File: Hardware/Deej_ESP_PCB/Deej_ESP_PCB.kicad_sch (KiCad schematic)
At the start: 124 parts, among them J1 USB_C_Receptacle_USB2.0_16P, P1 10K, P2 10K, P3 10K, P4 10K, P5 10K, P6 10K, SW1 SW_Push, SW2 SW_Push, SW3 SW_Push, SW4 SW_Push, SW5 SW_Push, SW6 SW_Push, U1 ESP32-S3-MINI-1U, U11 ECMF02-2AMX6, U12 LMS1585ACS-3.3/NOPB, U15 1.3" 128x64 OLED, U2 PCF8574RGTR, U3 PCF8574RGTR, U4 PCF8574RGTR, U5 SN74HCS126DR, U6 SN74HCS126DR, U7 1.3" 128x64 OLED, U8 1.3" 128x64 OLED, U9 1.3" 128x64 OLED

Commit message: Migrated Project Footprints to KiCAD Stable
- I updated the project footprints to be compatable with KiCAD stable
  release.
- I replaced the footprint for the slide potentiometer.
- I corrected the Adafruit display in the BOM sheet since I swapped it
  out a few commits ago.
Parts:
- P1, P2, P3, P4, P5, P6: footprint Bourns_Potentiometer:PTL01 -> Bourns_Potentiometer:PTL0115R0103B1

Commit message: Still dealing with KiCAD Migration issues
- Had to spend way too much time fixing the libraries.
- Adjusted the Adafruit 1.3" OLED footprint 3D model to use a lower
  profile pin headder.
- Added the lower profile pins to the BOM.
- Went through some of the ERC and fixed some issues (most relating to
  the library issues mentioned above).
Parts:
- removed D25: Green LED, LED_SMD:LED_0603_1608Metric_Pad1.05x0.95mm_HandSolder, symbol Device:LED
- removed R29: 100, Capacitor_SMD:C_0603_1608Metric_Pad1.08x0.95mm_HandSolder, symbol Device:R
- removed U2, U3, U4: PCF8574RGTR, RGT16_1P6X1P6, symbol TI:PCF8574RGTR
- CR1: renamed from CR17; footprint QFN1610_STM -> STM:QFN-6L_STM
- CR10: renamed from CR2; footprint DIODE_ESDALC6V1-1U2_STM -> STM:DIODE_ESDALC6V1-1U2_STM
- CR11: renamed from CR1; footprint DIODE_ESDALC6V1-1U2_STM -> STM:DIODE_ESDALC6V1-1U2_STM
- CR12: renamed from CR11; footprint DIODE_ESDALC6V1-1U2_STM -> STM:DIODE_ESDALC6V1-1U2_STM
- CR13: renamed from CR12; footprint DIODE_ESDALC6V1-1U2_STM -> STM:DIODE_ESDALC6V1-1U2_STM
- CR14: renamed from CR13; footprint DIODE_ESDALC6V1-1U2_STM -> STM:DIODE_ESDALC6V1-1U2_STM
- CR15: renamed from CR14; footprint DIODE_ESDALC6V1-1U2_STM -> STM:DIODE_ESDALC6V1-1U2_STM
- CR16: renamed from CR15; footprint DIODE_ESDALC6V1-1U2_STM -> STM:DIODE_ESDALC6V1-1U2_STM
- CR17: renamed from CR16; footprint DIODE_ESDALC6V1-1U2_STM -> STM:DIODE_ESDALC6V1-1U2_STM
- CR2: renamed from CR10; footprint DIODE_ESDALC6V1-1U2_STM -> STM:DIODE_ESDALC6V1-1U2_STM
- CR3: renamed from CR9; footprint DIODE_ESDALC6V1-1U2_STM -> STM:DIODE_ESDALC6V1-1U2_STM
- CR4: renamed from CR8; footprint DIODE_ESDALC6V1-1U2_STM -> STM:DIODE_ESDALC6V1-1U2_STM
- CR5: renamed from CR7; footprint DIODE_ESDALC6V1-1U2_STM -> STM:DIODE_ESDALC6V1-1U2_STM
- CR6: footprint DIODE_ESDALC6V1-1U2_STM -> STM:DIODE_ESDALC6V1-1U2_STM
- CR7: renamed from CR5; footprint DIODE_ESDALC6V1-1U2_STM -> STM:DIODE_ESDALC6V1-1U2_STM
- CR8: renamed from CR4; footprint DIODE_ESDALC6V1-1U2_STM -> STM:DIODE_ESDALC6V1-1U2_STM
- CR9: renamed from CR3; footprint DIODE_ESDALC6V1-1U2_STM -> STM:DIODE_ESDALC6V1-1U2_STM
- U10: renamed from U8; footprint Adafruit_1_3_OLED -> Adafruit:Adafruit_1_3_OLED
- U11: renamed from U9; footprint Adafruit_1_3_OLED -> Adafruit:Adafruit_1_3_OLED
- U4: renamed from U14; value ~ -> 10K
- U5: renamed from U13; value ~ -> 10K
- U6: renamed from U5; footprint D0014A-IPC_A -> TI:D0014A-IPC_A
- U7: renamed from U6; footprint D0014A-IPC_A -> TI:D0014A-IPC_A
- U8: renamed from U15; footprint Adafruit_1_3_OLED -> Adafruit:Adafruit_1_3_OLED
- U9: renamed from U7; footprint Adafruit_1_3_OLED -> Adafruit:Adafruit_1_3_OLED
- renumbered C25 to C1, C6 to C10, C1 to C11, C3 to C12, C14 to C13, C21 to C14, C22 to C16, C9 to C17, C16 to C18, C23 to C19, C11 to C2, C7 to C20, C2 to C21, C4 to C22, C8 to C23, C17 to C24, C24 to C25, C10 to C26, C18 to C3, C26 to C4, C12 to C5, C19 to C6, C13 to C7, C20 to C8, C5 to C9, D23 to D1, D20 to D10, D3 to D11, D8 to D12, D1 to D13, D4 to D14, D21 to D16, D16 to D17, D22 to D18, D5 to D19, D11 to D2, D7 to D20, D9 to D21, D2 to D22, D6 to D23, D10 to D24, D17 to D3, D12 to D4, D18 to D5, D24 to D6, D13 to D7, D19 to D8, D14 to D9, P3 to P2, P5 to P3, P2 to P4, P4 to P5, R25 to R1, R13 to R10, R15 to R11, R1 to R12, R7 to R13, R21 to R14, R6 to R15, R12 to R16, R22 to R17, R24 to R18, R18 to R19, R26 to R2, R5 to R20, R11 to R21, R19 to R22, R2 to R23, R8 to R24, R17 to R25, R3 to R26, R10 to R27, R20 to R28, R27 to R3, R23 to R4, R28 to R5, R14 to R6, R16 to R7, R4 to R8, SW3 to SW2, SW5 to SW3, SW2 to SW4, SW4 to SW5, U11 to U1, U1 to U2, U12 to U3
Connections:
- net IO0 is gone; now on net MuteSW_0: U2.4 (IO0)
- net IO1 is gone; now on net SCLK: U2.5 (IO1)
- net IO10 is gone; now on net Analog_1: U2.14 (IO10)
- net IO11 is gone; now on net Analog_2: U2.15 (IO11)
- net IO12 is gone; now on net Analog_3: U2.16 (IO12)
- net IO13 is gone; now on net Analog_4: U2.17 (IO13)
- net IO14 is gone; now on net Analog_5: U2.18 (IO14)
- net IO15 is gone; now on net Analog_6: U2.19 (IO15)
- net IO16 is gone; now on net Analog_7: U2.20 (IO16)
- net IO17 is gone; now on net NEOLED: U2.21 (IO17)
- net IO18 is gone; now on net MuteLED_2: U2.22 (IO18)
- net IO2 is gone; now on net MOSI: U2.6 (IO2)
- net IO21 is gone; now on net MuteLED_3: U2.25 (IO21)
- net IO26 is gone; now on net MuteLED_4: U2.26 (IO26)
- net IO3 is gone; now on net D/C: U2.7 (IO3)
- net IO33 is gone; now on net MuteLED_5: U2.28 (IO33)
- net IO34 is gone; now on net MuteLED_6: U2.29 (IO34)
- net IO37 is gone; now on net MuteSW_2: U2.33 (IO37)
- net IO38 is gone; now on net MuteSW_3: U2.34 (IO38)
- net IO39 is gone; now on net MuteSW_4: U2.35 (IO39)
- net IO4 is gone; now on net RST: U2.8 (IO4)
- net IO40 is gone; now on net MuteSW_5: U2.36 (IO40)
- net IO41 is gone; now on net MuteSW_6: U2.37 (IO41)
- net IO42 is gone; now on net MuteSW_7: U2.38 (IO42)
- net IO5 is gone; now on net CS0: U2.9 (IO5)
- net IO6 is gone; now on net CS1: U2.10 (IO6)
- net IO7 is gone; now on net CS2: U2.11 (IO7)
- net IO8 is gone; now on net CS3: U2.12 (IO8)
- net IO9 is gone; now on net Analog_0: U2.13 (IO9)
- net IO35: now also U2.39 (TXD0); no longer U2.31 (IO35)
- net IO36: now also U2.40 (RXD0); no longer U2.32 (IO36)
- net MuteLED_7: now also U2.31 (IO35)
- net MuteSW_1: now also U2.32 (IO36)
- net IO45: no longer names the net of U2.41 (IO45)
- net IO46: no longer names the net of U2.44 (IO46)
- net IO47: no longer names the net of U2.27 (IO47)
- net IO48: no longer names the net of U2.30 (IO48)

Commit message: Finished Schemtic 🎉      For now...
- Added supporting hardware for the ESP32-S3 (decoupling capacitors and
  reset button)
- Added hardware support for a UART conntection (hoping I won't need to
  use it but you never know)
- Fixed all ERC issues
- Replaced the original 11mm stand offs with 8mm stand offs for the
  Adafruit displays
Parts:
- added C1, C4: 0.1uF, Capacitor_SMD:C_0603_1608Metric_Pad1.08x0.95mm_HandSolder, symbol Device:C
- added C2: 1uF, Capacitor_SMD:C_0603_1608Metric_Pad1.08x0.95mm_HandSolder, symbol Device:C
- added C3: 22uF, Capacitor_SMD:C_0603_1608Metric_Pad1.08x0.95mm_HandSolder, symbol Device:C
- added D25: Orange LED, LED_SMD:LED_0603_1608Metric_Pad1.05x0.95mm_HandSolder, symbol Device:LED
- added D26: Green LED, LED_SMD:LED_0603_1608Metric_Pad1.05x0.95mm_HandSolder, symbol Device:LED
- added J2: UART Header, Connector_PinHeader_2.54mm:PinHeader_1x04_P2.54mm_Vertical, symbol Connector:Conn_01x04_Pin
- added R1: 10K, Capacitor_SMD:C_0603_1608Metric_Pad1.08x0.95mm_HandSolder, symbol Device:R
- added R24: 100, Capacitor_SMD:C_0603_1608Metric_Pad1.08x0.95mm_HandSolder, symbol Device:R
- added R25: 5, Capacitor_SMD:C_0603_1608Metric_Pad1.08x0.95mm_HandSolder, symbol Device:R
- added SW1: Reset, TEConnectivity:SWITCH_FSMSM_TYC, symbol Switch:SW_Push
- renumbered C6 to C10, C7 to C11, C8 to C12, C9 to C13, C10 to C14, C11 to C15, C12 to C16, C13 to C17, C14 to C18, C15 to C19, C16 to C20, C17 to C21, C18 to C22, C19 to C23, C20 to C24, C21 to C25, C22 to C26, C23 to C27, C24 to C28, C25 to C29, C26 to C30, C1 to C5, C2 to C6, C3 to C7, C4 to C8, C5 to C9, R9 to R10, R10 to R11, R11 to R12, R12 to R13, R13 to R14, R14 to R15, R15 to R16, R16 to R17, R17 to R18, R18 to R19, R1 to R2, R19 to R20, R20 to R21, R21 to R22, R22 to R23, R23 to R26, R24 to R27, R25 to R28, R26 to R29, R2 to R3, R27 to R30, R28 to R31, R3 to R4, R4 to R5, R5 to R6, R6 to R7, R7 to R8, R8 to R9, SW1 to SW2, SW2 to SW3, SW3 to SW4, SW4 to SW5, SW5 to SW6, SW6 to SW7
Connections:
- net MuteLED_7 is gone; now on net MuteLED_6: P6.E1, U2.31 (IO35)
- net +3.3V: now also U2.3 (3V3), C3.1, C4.1, J2.1 (Pin_1), R1.2, R24.1, R25.1
- net GND: now also R19.2, U2.1 (GND), U2.2 (GND), U2.42 (GND), U2.43 (GND), U2.46 (GND), U2.47 (GND), U2.48 (GND), U2.49 (GND), U2.50 (GND), U2.51 (GND), U2.52 (GND), U2.53 (GND), U2.54 (GND), U2.55 (GND), U2.56 (GND), U2.57 (GND), U2.58 (GND), U2.59 (GND), U2.60 (GND), U2.61 (GND), U2.62 (GND), U2.63 (GND), U2.64 (GND), U2.65 (GND), C1.2, C2.2, C3.2, C4.2, J2.4 (Pin_4), SW1.1
- net MuteLED_2: now also P2.E1, U2.25 (IO21); no longer P1.E1, U2.22 (IO18)
- net MuteLED_3: now also P3.E1, U2.26 (IO26); no longer P2.E1, U2.25 (IO21)
- net MuteLED_4: now also P4.E1, U2.28 (IO33); no longer P3.E1, U2.26 (IO26)
- net MuteLED_5: now also P5.E1, U2.29 (IO34); no longer P4.E1, U2.28 (IO33)
- net MuteLED_6: no longer P5.E1, U2.29 (IO34)
- net RX_LED: now reaches U2.27 (IO47)
- net RX_LED: now also D25.1 (K)
- net TX_LED: now reaches U2.30 (IO48)
- net TX_LED: now also D26.1 (K)
- net at U2.45 (EN): now also C1.1, C2.1, R1.1, SW1.2
- net IO35 renamed UART_TX
- net UART_TX: now also J2.3 (Pin_3)
- net IO36 renamed UART_RX
- net UART_RX: now also J2.2 (Pin_2)
- net NEOLED renamed NEOLED_0
- new net: D26.2 (A), R25.2
- new net: D25.2 (A), R24.2
- new net MuteLED_1: P1.E1, U2.22 (IO18)
- no-connect marks 3 -> 5
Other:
- moved on the sheet: U2

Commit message: Synced the KiCAD BOM and my handmade BOM
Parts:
- added C3, C31, C32, C33, C34, C35, C36, C5: 0.1uF, Capacitor_Tantalum_SMD:CP_EIA-3216-18_Kemet-A_HandSolder, symbol Device:C_Polarized
- D18: renamed from D21; value D -> MMSD4148T1G
- D19: renamed from D22; value D -> MMSD4148T1G
- D20: renamed from D23; value D -> MMSD4148T1G
- D21: renamed from D24; value D -> MMSD4148T1G
- D5: renamed from D11; value D -> MMSD4148T1G
- D6: renamed from D12; value D -> MMSD4148T1G
- D7: renamed from D13; value D -> MMSD4148T1G
- D8: renamed from D14; value D -> MMSD4148T1G
- R24: renamed from R25; value 5 -> 10
- renumbered C6 to C1, C21 to C13, C17 to C14, C18 to C15, C5 to C16, C24 to C17, C25 to C18, C26 to C19, C7 to C2, C27 to C20, C19 to C21, C20 to C22, C8 to C23, C22 to C24, C23 to C25, C30 to C26, C28 to C27, C29 to C28, C1 to C29, C2 to C30, C3 to C37, C4 to C38, C13 to C4, C14 to C6, C15 to C7, C16 to C8, CR2 to CR1, CR3 to CR2, CR4 to CR3, CR5 to CR4, CR6 to CR5, CR7 to CR6, CR1 to CR7, D2 to D1, D8 to D10, D9 to D11, D10 to D12, D1 to D13, D15 to D14, D16 to D15, D17 to D16, D18 to D17, D3 to D2, D6 to D22, D19 to D23, D20 to D24, D4 to D3, D5 to D4, D7 to D9, R5 to R1, R2 to R10, R3 to R11, R4 to R12, R15 to R13, R16 to R14, R17 to R15, R18 to R16, R20 to R17, R21 to R18, R22 to R19, R7 to R2, R23 to R20, R6 to R21, R19 to R22, R24 to R23, R1 to R25, R8 to R3, R9 to R4, R10 to R5, R11 to R6, R12 to R7, R13 to R8, R14 to R9, SW2 to SW1, SW3 to SW2, SW4 to SW3, SW5 to SW4, SW6 to SW5, SW7 to SW6, SW1 to SW7, U4 to U1, U5 to U2, U1 to U3, U6 to U4, U3 to U5, U7 to U6, U2 to U7
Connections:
- net +3.3V: now also C3.1, C31.1, C32.1, C33.1, C34.1, C35.1, C36.1, C5.1
- net GND: now also C3.2, C31.2, C32.2, C33.2, C34.2, C35.2, C36.2, C5.2
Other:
- note added: "1.3" 128x64 OLEDs"
- note added: "ESP32-S3 Microprocessor"
- note added: "Linear Potentiometer"
- note added: "Power Input, Filtering, & Stepdown"
- note added: "Push Buttons W/ Hardware Debounce Primary Rotary Potentiometers"
- note added: "RX/TX LEDs"
- note added: "Rotary Potentiometer Mute LEDs % or dB select LEDs"
- moved on the sheet: C1, C10, C11, C12, C13, C14, C15, C17, C18, C19, C2, C20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

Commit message: Started PCB Layout Added Mounting Holes and Knobs
- Started doing PCB layout. I have an idea of large component placement
  and therefore overall board size but still working out finalizing
  them.
- Added platted mounting holes to the board mostly for support since
  most of this board is user interfaces I expect there to be a good
  amount of force applied to the sliders, buttons, and knobs.
- Found some metal knobs for the rotary potentiometers and added them to
  the custom BOM.
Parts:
- removed R22: 499, Capacitor_SMD:C_0603_1608Metric_Pad1.08x0.95mm_HandSolder, symbol Device:R
- added H1, H2, H3, H4, H5: ~, MountingHole:MountingHole_3.2mm_M3_Pad, symbol Mechanical:MountingHole_Pad
- added H10, H11, H12, H6, H7, H8, H9: MountingHole_Pad, MountingHole:MountingHole_3.2mm_M3_Pad, symbol Mechanical:MountingHole_Pad
- CR7: footprint STM:QFN-6L_STM -> STM:QFN1610_STM
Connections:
- net GND: now also U7.66 (GND), U7.67 (GND), U7.68 (GND), U7.69 (GND), U7.70 (GND), U7.71 (GND), U7.72 (GND), U7.73 (GND), H1.1, H10.1, H11.1, H12.1, H2.1, H3.1, H4.1, H5.1, H6.1, H7.1, H8.1, H9.1
- net at D19.2 (A), R14.1, R18.2: now also SW2.2; no longer SW4.2
- net at D7.2 (A), R4.1, R8.2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: now also SW6.2; no longer SW1.2
- net at D8.2 (A), R5.1, R9.2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: now also SW5.2; no longer SW2.2
- net at D21.2 (A), R16.1, R20.2: now also SW4.2; no longer SW6.2
- net at D20.2 (A), R15.1, R19.2: now also SW3.2; no longer SW5.2
- net at D18.2 (A), R13.1, R17.2: now also SW1.2; no longer SW3.2
- no-connect marks 5 -> 6
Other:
- moved on the sheet: SW1, SW2, SW3, SW4, SW5, SW6

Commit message: All Components Placed and OSH Park Rules Set.
- I have placed all of the components and I am looking at starting trace
  layout.
- I have also set the rules and board stack up specifications for OSH
  Park to ensure thaat the design is as similr to how the final product
  will be.
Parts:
- renumbered H11 to H10, H6 to H11, H7 to H2, H2 to H3, H8 to H4, H3 to H5, H9 to H6, H4 to H7, H10 to H8, H5 to H9, R23 to R22, R24 to R23, R25 to R24, R26 to R25, R27 to R26, R28 to R27, R29 to R28, R30 to R29, R31 to R30, SW6 to SW1, SW5 to SW2, SW1 to SW3, SW2 to SW4, SW3 to SW5, SW4 to SW6

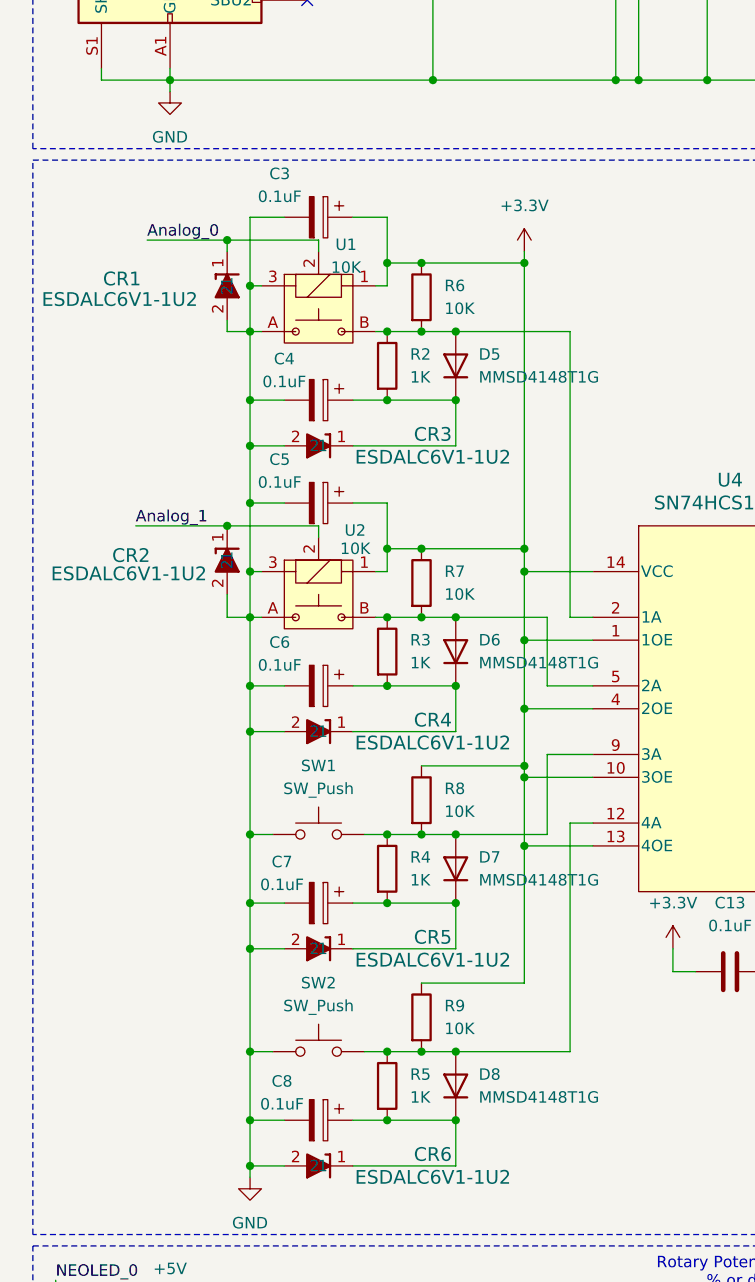
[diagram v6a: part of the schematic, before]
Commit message: More Power Routing and NEO Pixel LED Routing
- Added more +3.3V voltage routing
- Added some signaling for the NEO Pixel LEDs

TODO: Other LED traces and analog dials
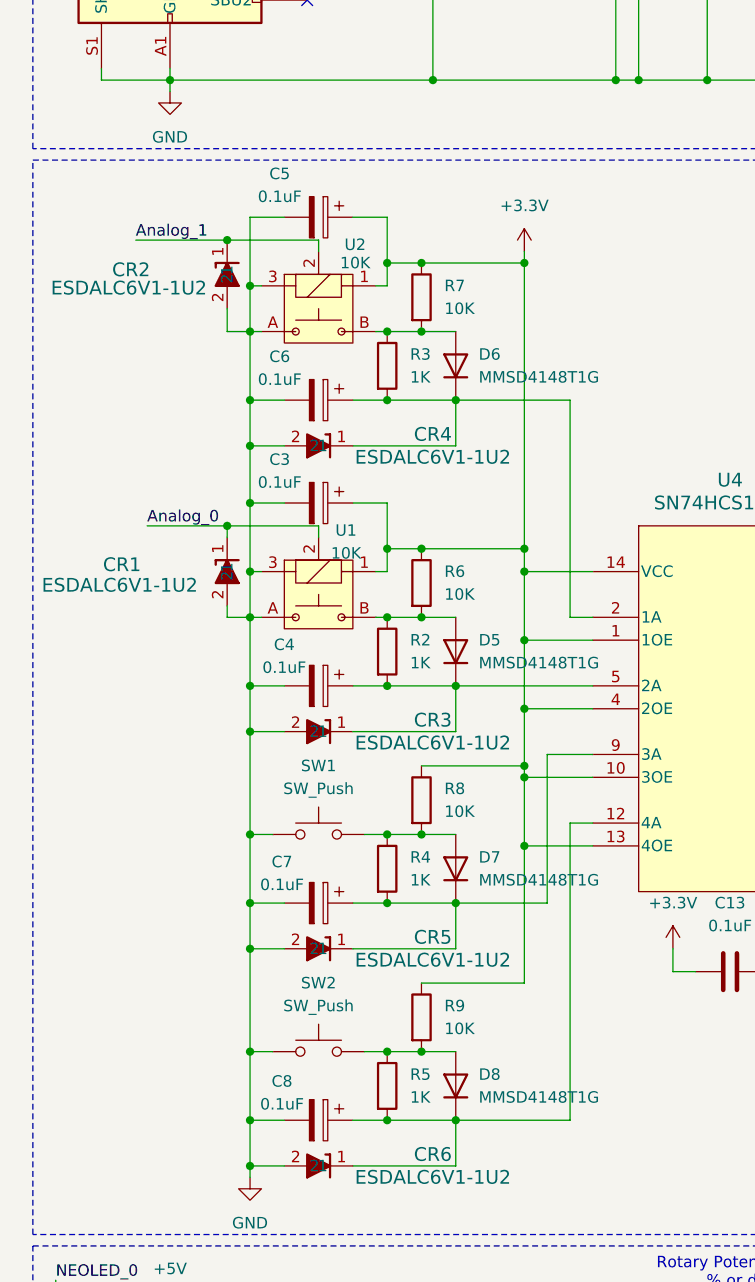
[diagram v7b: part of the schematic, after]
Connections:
- net at C6.1, CR4.1, D6.1 (K)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: now also U4.2 (1A)
- net at D6.2 (A), R3.1, R7.2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: no longer U4.5 (2A)
- net at D8.2 (A), R5.1, R9.2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: no longer U4.12 (4A)
- net at C8.1, CR6.1, D8.1 (K)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: now also U4.12 (4A)
- net at C7.1, CR5.1, D7.1 (K)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: now also U4.9 (3A)
- net at D7.2 (A), R4.1, R8.2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: no longer U4.9 (3A)
- net at D5.2 (A), R2.1, R6.2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: no longer U4.2 (1A)
- net at C4.1, CR3.1, D5.1 (K)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: now also U4.5 (2A)
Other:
- moved on the sheet: C3, C4, C5, C6, CR1, CR2, CR3, CR4, D5, D6, R2, R3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

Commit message: Finished Running Traces, On to DRC Fixes
- I believe I finished running the traces to get everything connected
  KiCAD shows one more air wire but that seems like a visual isses since
  I can confirm it is connected.
- Next I will be starting on fixing the 94 DRC ERRORs. A lot of them
  seems really simple on first glance so I'm not worried about those but
  there are a few errors involving clearances and manufacturing minimums.
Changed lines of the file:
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@@
 		)
 	)
-	(text_box "Audio Controller Hardware\nThis Schematic gives a user the ability to use hardware potentiometers and pushbuttons to control their PC audio.\nThe system takes in power from the USB C port and converts it form 5V to 3.3V.\nThe ESP32-S3 selected has built in Bluetooth and WiFi which allows wireless connectivity if software changes enable it's use.\nAll Push buttons have hardware filtering and debouncing (I didn't feel like doing it in software and also wanted to learn how it's done).\nPotentiameters have decoupling on their power inputs to reduce noise (unessecarry for the application but felt like exprimenting).\nNeoPixel LEDs are for noting the selection between % and dB for sliders.\nOLEDs are for giving more complex user feed back."
+	(text_box "Audio Controller Hardware\nThis Schematic gives a user the ability to use hardware potentiometers and pushbuttons to control their PC audio.\nThe system takes in power from the USB C port and converts it form 5V to 3.3V.\nThe ESP32-S3 selected has built in Bluetooth and WiFi which allows wireless connectivity if software changes enable its use.\nAll Push buttons have hardware filtering and debouncing (I didn't feel like doing it in software and also wanted to learn how it's done).\nPotentiameters have decoupling on their power inputs to reduce noise (unessecarry for the application but felt like exprimenting).\nNeoPixel LEDs are for noting the selection between % and dB for sliders.\nOLEDs are for giving more complex user feed back."
 		(exclude_from_sim no)
 		(at 203.2 95.25 0)
